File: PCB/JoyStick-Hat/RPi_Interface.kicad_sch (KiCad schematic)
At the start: 13 parts, among them J7 Raspberry_Pi_2_3

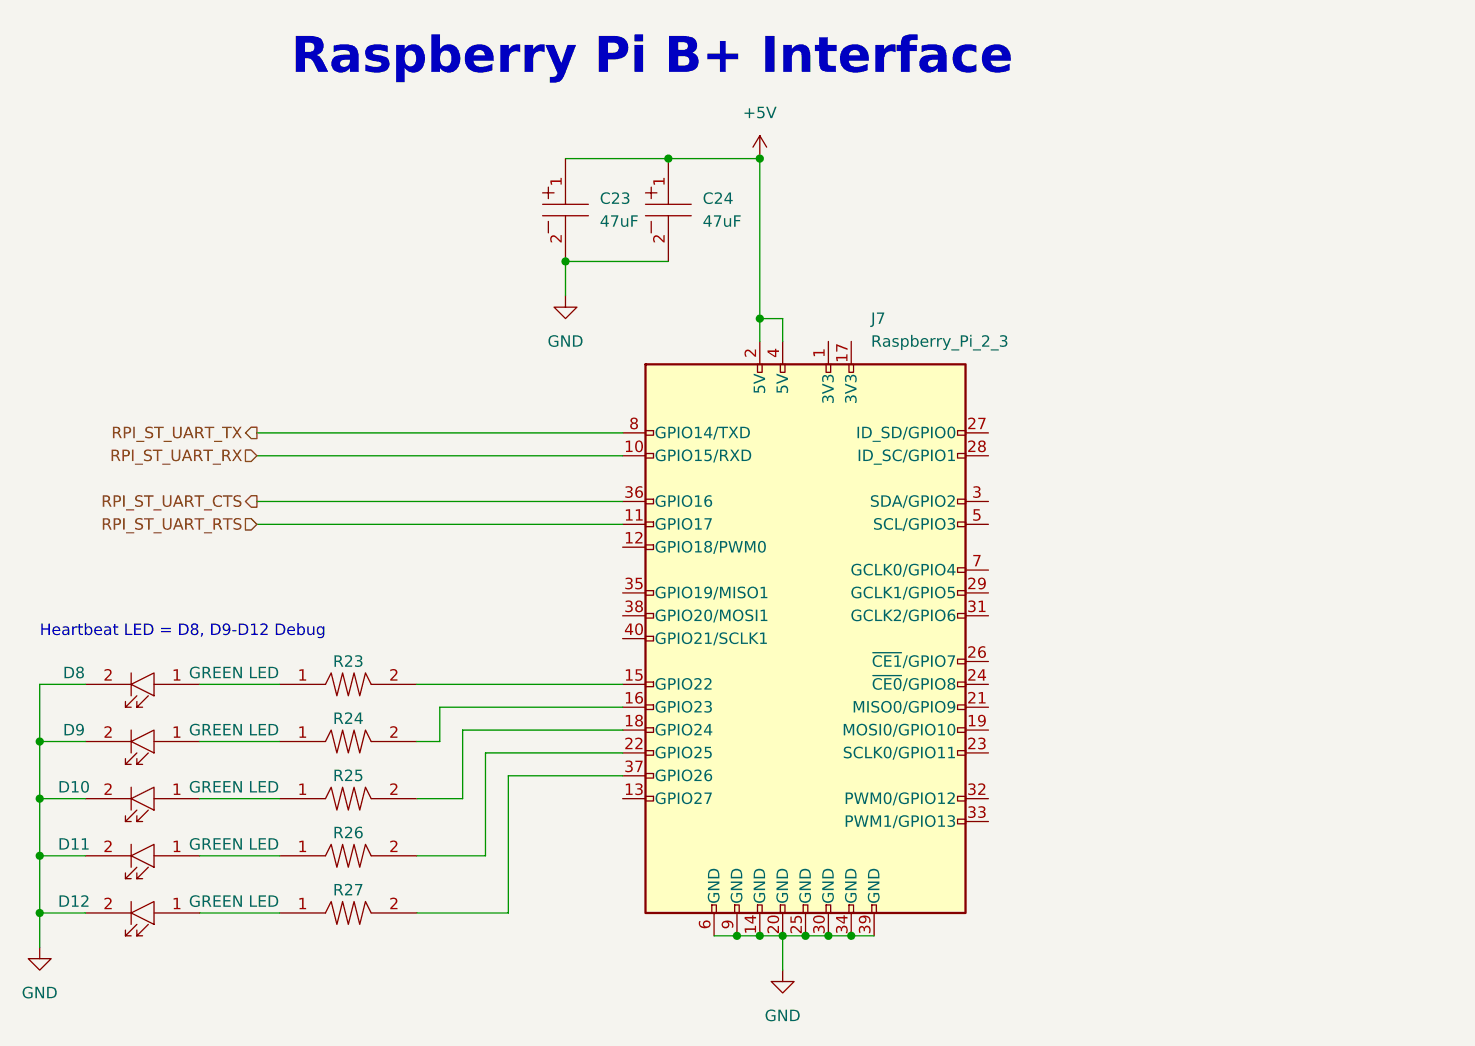
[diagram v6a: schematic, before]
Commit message: PCB First Pass Complete
First complete pass at PCB finished. Added more debug LEDs for both STM32 and RPi, 8 totaly so binary data can be outputted as a byte etc, that way we can have debug codes. Added heartbeat LED to STM32. Rearranged connectors and pinning of certain connectors to make routing smooth and traces short.
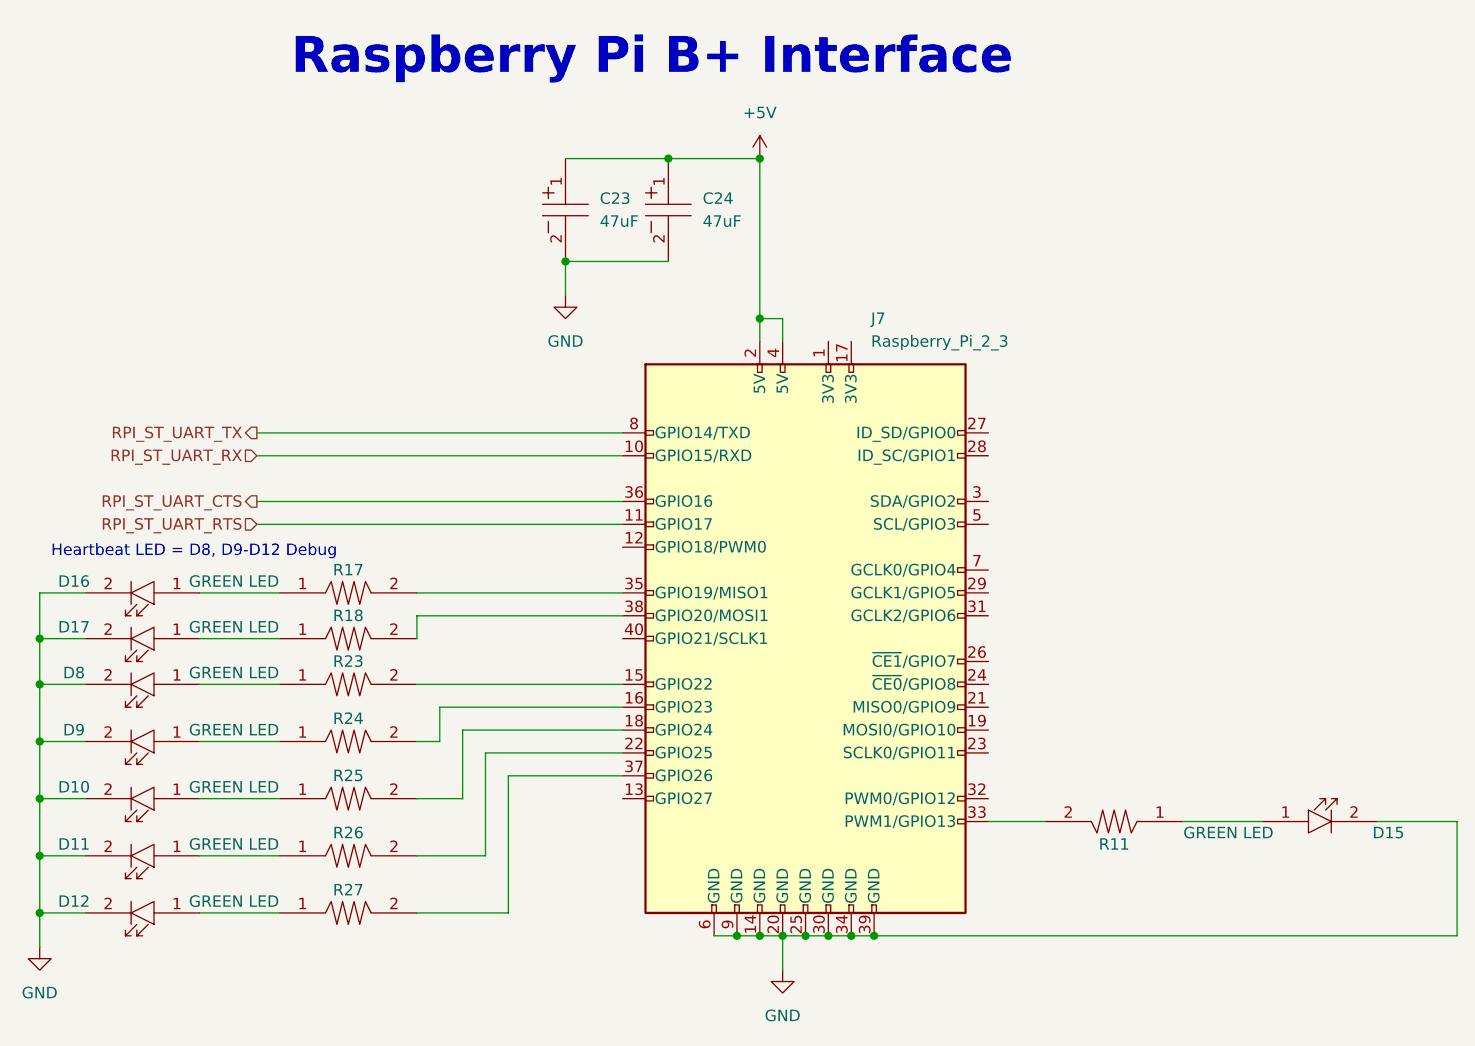
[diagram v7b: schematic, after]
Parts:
- added D15, D16, D17: LTST-C194KGKT, AVR-KiCAD-Lib-Diodes:LED0603, symbol AVR-KiCAD-Lib-Diodes:LTST-C194KGKT
- added R11, R17, R18: RC0603FR-07470RL, AVR-KiCAD-Lib-Resistors:R0603, symbol AVR-KiCAD-Lib-Resistors:RC0603FR-07470RL
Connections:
- net GND: now also D15.2, D16.2, D17.2
- net at J7.33 (PWM1/GPIO13): now also R11.2
- net at J7.35 (GPIO19/MISO1): now also R17.2
- net at J7.38 (GPIO20/MOSI1): now also R18.2
- new net: D16.1, R17.1
- new net: D17.1, R18.1
- new net: D15.1, R11.1

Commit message: James Fixes and 3D models
Added all the changes that James suggested to the design and then added 3D models to the board for mechanical design purposes. Generated 3D renders of the board and added them to new directory called img.
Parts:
- J7: footprint AVR-KiCAD-Lib-Connectors:PinHeader_2x21_P2.54mm_Vertical -> AVR-KiCAD-Lib-Connectors:PinHeader_2x21_P2.54mm_Female_Bottom
